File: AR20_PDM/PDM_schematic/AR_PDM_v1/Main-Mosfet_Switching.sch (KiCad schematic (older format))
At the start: 57 parts, among them SW1 SW_DIP_x07, U15 NMOS, U16 NMOS, U17 NMOS, U18 NMOS, U19 NMOS, U20 NMOS, U21 NMOS, U22 NMOS, U23 NMOS, U24 NMOS, U25 NMOS, U26 NMOS, U27 NMOS, U28 NMOS

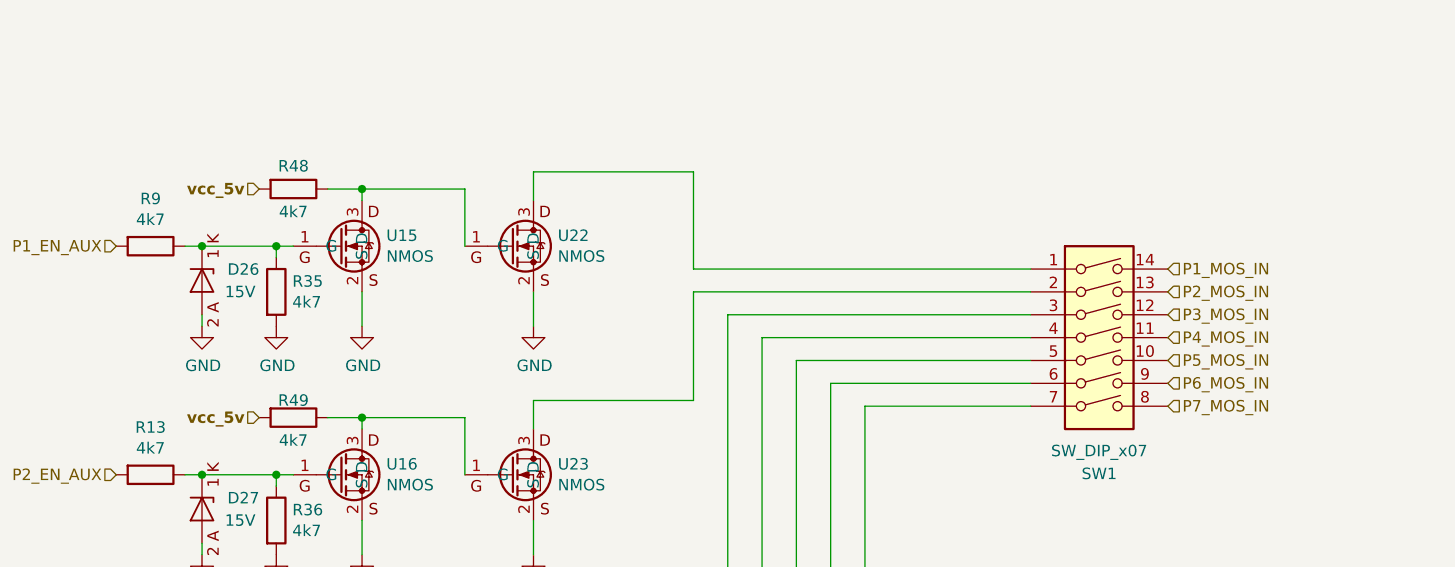
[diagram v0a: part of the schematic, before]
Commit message: All components in place - PCB work in progress
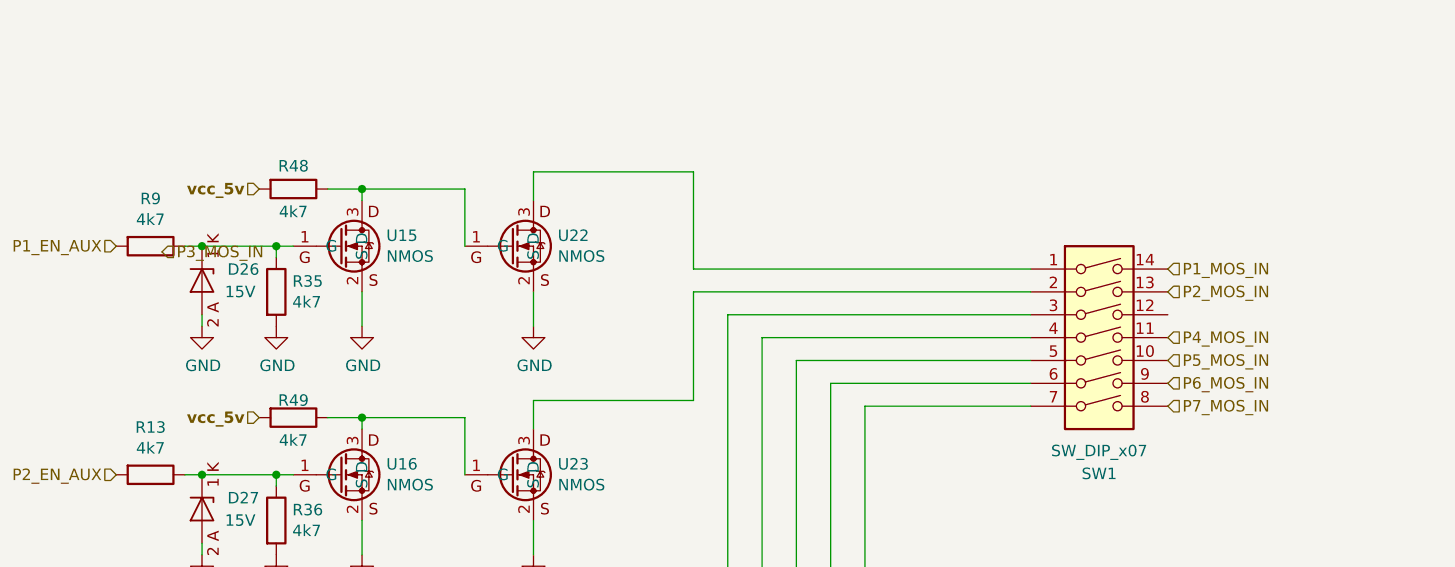
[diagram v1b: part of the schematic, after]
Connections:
- net P3_MOS_IN: no longer SW1.12
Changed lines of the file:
@@
 $Descr A4 11693 8268
 encoding utf-8
-Sheet 13 14
+Sheet 12 14
 Title ""
 Date ""
@@
 Text HLabel 5700 1200 2    50   Input ~ 0
 P2_MOS_IN
-Text HLabel 5700 1300 2    50   Input ~ 0
-P3_MOS_IN
 Text HLabel 5700 1400 2    50   Input ~ 0
 P4_MOS_IN
@@
 Wire Wire Line
 	3625 675  3625 1100
-Wire Wire Line
-	5100 1100 3625 1100
 Text Notes 5325 3000 0    50   ~ 0
 Protected AUX Input stages,\nwith Nmos resistive inverter \nand Nmos to controll the "in" signal of the BIG mosfet\n\nDip switch is to disable AUX inputs. \n
@@
 Text HLabel 9475 5200 2    50   Input ~ 0
 P7_EN_ACM
+Text HLabel 1300 1025 2    50   Input ~ 0
+P3_MOS_IN
+Wire Wire Line
+	5100 1100 3625 1100
 $EndSCHEMATC

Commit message: Pdm version B Draft finished
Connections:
- net P3_MOS_IN: now also SW1.12
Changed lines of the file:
@@
 Text HLabel 5700 1200 2    50   Input ~ 0
 P2_MOS_IN
-Text HLabel 5700 1400 2    50   Input ~ 0
-P4_MOS_IN
 Text HLabel 5700 1500 2    50   Input ~ 0
 P5_MOS_IN
@@
 Wire Wire Line
 	5100 1100 3625 1100
+Text HLabel 5700 1400 2    50   Input ~ 0
+P4_MOS_IN
+Text HLabel 5700 1300 2    50   Input ~ 0
+P3_MOS_IN
 $EndSCHEMATC

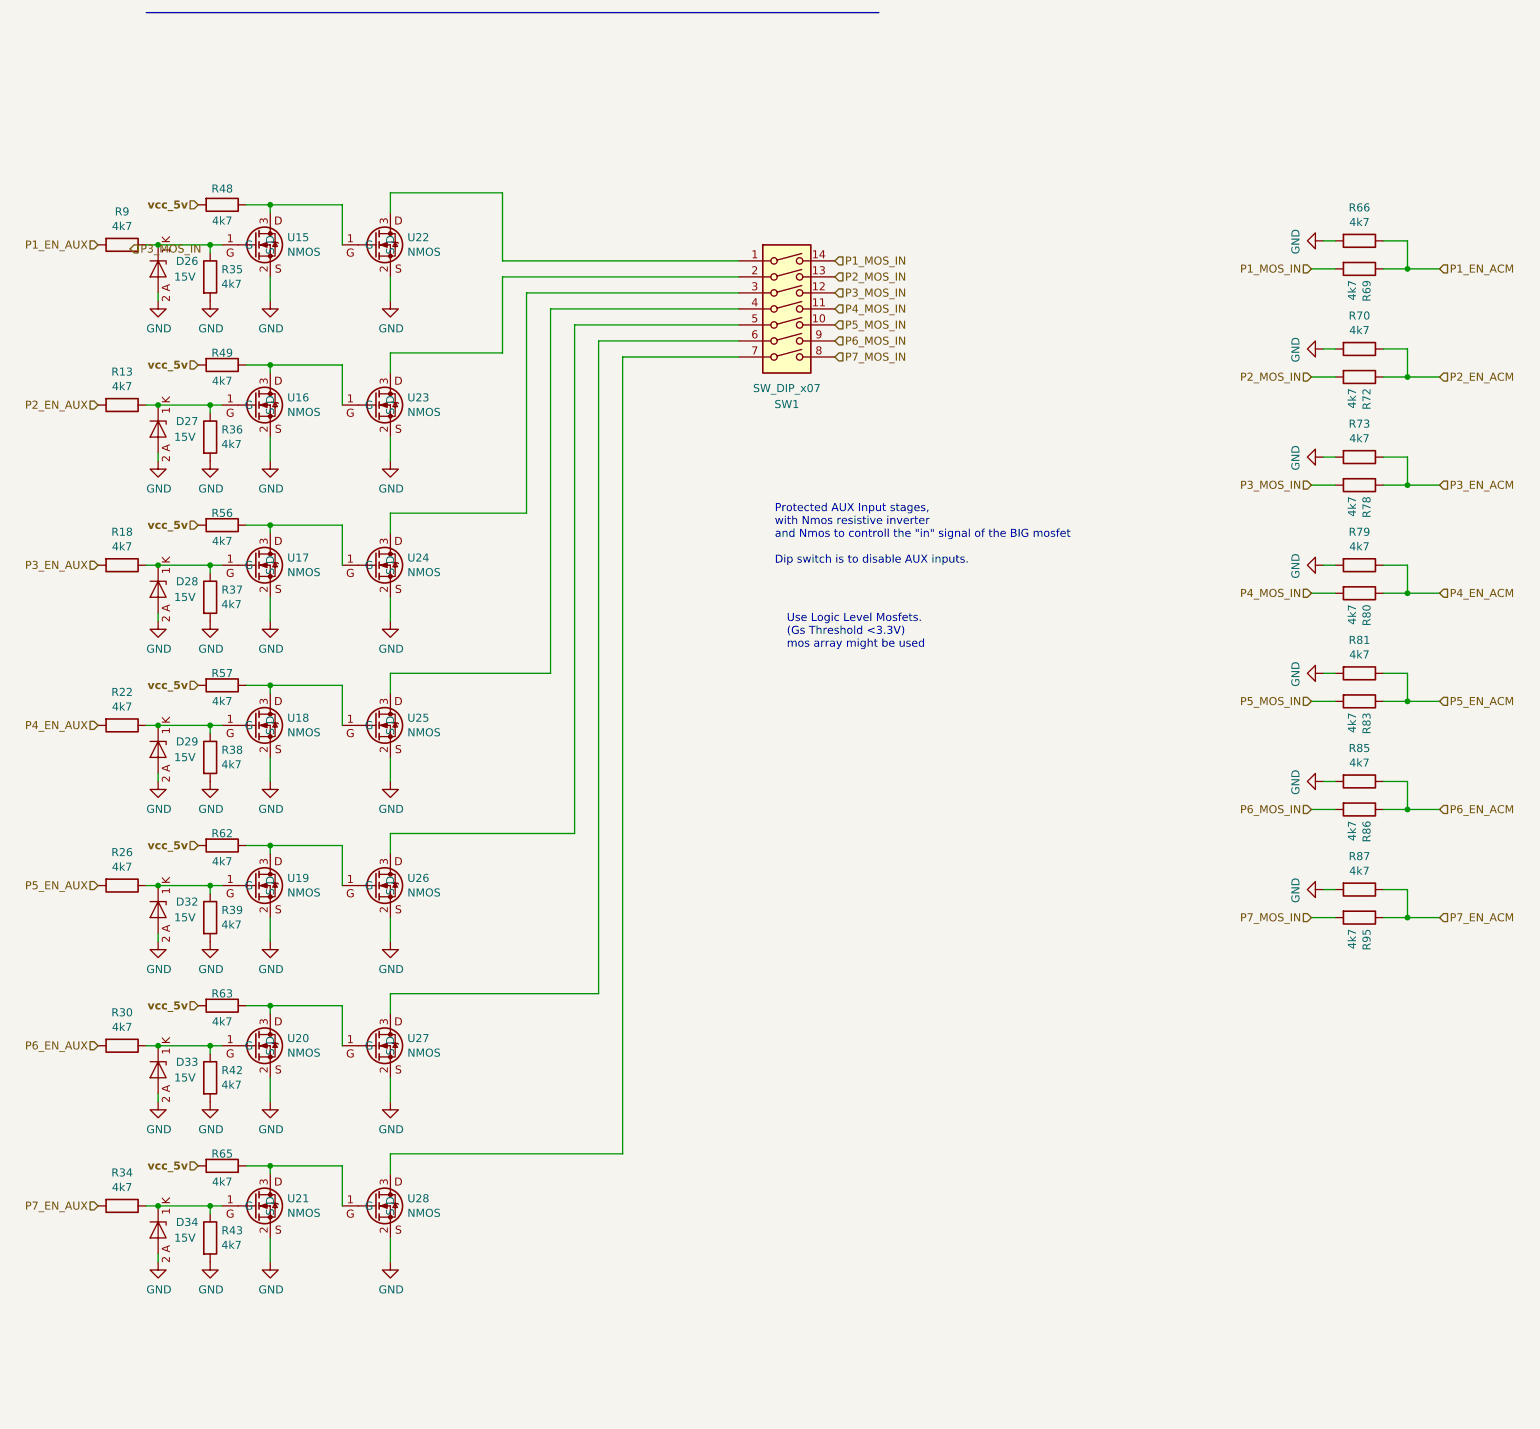
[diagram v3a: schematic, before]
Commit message: Further testing, reveals pdm needs rework
-  As of now, there are major errors in schematics.
- Needs rework. Version charlie postponed.
- Very nice pcb layout thats almost finished. 
   worth noting this layout for the future
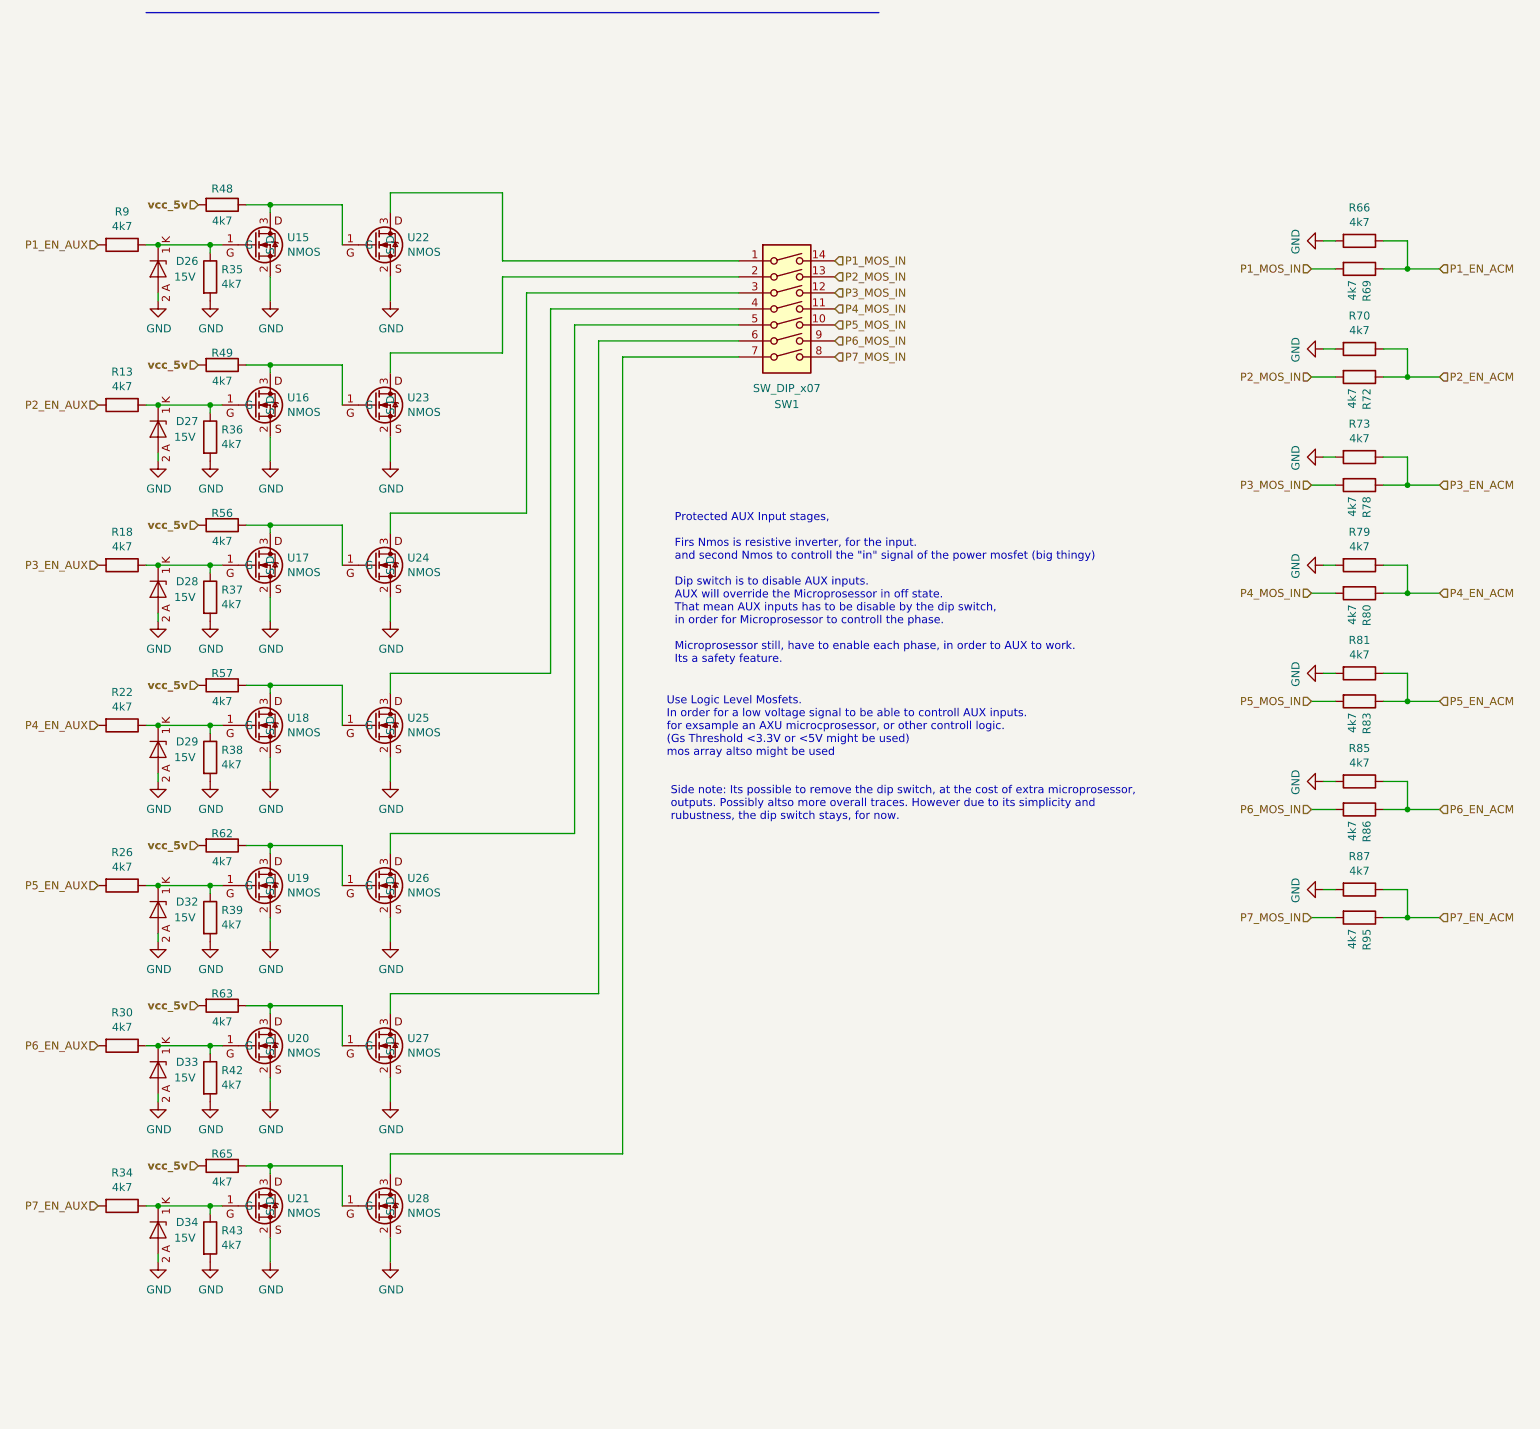
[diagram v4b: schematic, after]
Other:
- note added: "Protected AUX Input stages,\n\nFirs Nmos is resistive inverter, for the input.\nand second Nmos to controll the "in" signal of the power mosfet (big thingy)\n\nDip switch is to disable AUX inputs. \nAUX will override the Microprosessor in off state. \nThat mean AUX inputs has to be disable by the dip switch, \nin order for Microprosessor to controll the phase.\n\nMicroprosessor still, have to ena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"
- note added: "Side note: Its possible to remove the dip switch, at the cost of extra microprosessor, \noutputs. Possibly altso more overall traces. However due to its simplicity and \nrubustness, the dip switch stays, for now. \n"
- note added: "Use Logic Level Mosfets. \nIn order for a low voltage signal to be able to controll AUX inputs.\nfor exsample an AXU microcprosessor, or other controll logic.\n(Gs Threshold <3.3V or <5V might be used)\nmos array altso might be used"
- note removed: "Protected AUX Input stages,\nwith Nmos resistive inverter \nand Nmos to controll the "in" signal of the BIG mosfet\n\nDip switch is to disable AUX inputs. \n"
- note removed: "Use Logic Level Mosfets. \n(Gs Threshold <3.3V)\nmos array might be used"
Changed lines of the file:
@@
 Text HLabel 5700 1700 2    50   Input ~ 0
 P7_MOS_IN
-Text Notes 5400 3525 0    50   ~ 0
-Use Logic Level Mosfets. \n(Gs Threshold <3.3V)\nmos array might be used
+Text Notes 4650 4200 0    50   ~ 0
+Use Logic Level Mosfets. \nIn order for a low voltage signal to be able to controll AUX inputs.\nfor exsample an AXU microcprosessor, or other controll logic.\n(Gs Threshold <3.3V or <5V might be used)\nmos array altso might be used
 $Comp
 L AR20_PDM_v1-rescue:N-MOS-DMN6140L-13 U?
@@
 Wire Wire Line
 	3625 675  3625 1100
-Text Notes 5325 3000 0    50   ~ 0
-Protected AUX Input stages,\nwith Nmos resistive inverter \nand Nmos to controll the "in" signal of the BIG mosfet\n\nDip switch is to disable AUX inputs. \n
+Text Notes 4700 3700 0    50   ~ 0
+Protected AUX Input stages,\n\nFirs Nmos is resistive inverter, for the input.\nand second Nmos to controll the "in" signal of the power mosfet (big thingy)\n\nDip switch is to disable AUX inputs. \nAUX will override the Microprosessor in off state. \nThat mean AUX inputs has to be disable by the dip switch, \nin order for Microprosessor to controll the phase.\n\nMicroprosessor still, have to enable each phase, in order to AUX to work.\nIts a safety feature. \n\n
 Wire Wire Line
 	9125 975  9275 975
@@
 Text HLabel 9475 5200 2    50   Input ~ 0
 P7_EN_ACM
-Text HLabel 1300 1025 2    50   Input ~ 0
-P3_MOS_IN
 Wire Wire Line
 	5100 1100 3625 1100
@@
 Text HLabel 5700 1300 2    50   Input ~ 0
 P3_MOS_IN
+Text Notes 4675 4600 0    50   ~ 0
+Side note: Its possible to remove the dip switch, at the cost of extra microprosessor, \noutputs. Possibly altso more overall traces. However due to its simplicity and \nrubustness, the dip switch stays, for now. \n
 $EndSCHEMATC
